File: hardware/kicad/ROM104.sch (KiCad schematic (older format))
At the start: 27 parts, among them J1 Screw_Terminal_01x12, J2 CAN, K1 DIPxx-1Cxx-51x, K2 DIPxx-1Cxx-51x, K3 DIPxx-1Cxx-51x, K4 DIPxx-1Cxx-51x, SW1 INSTANCE, SW2 BUS, U1 L293D, U2 MCP2551-I-P, U3 TMR-1211, U4 Teensy_3.2, U5 L293D

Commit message: Stuff
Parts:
- R12, R13, R14, R9: value 4K7 -> 470R
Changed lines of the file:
@@
 P 4400 800
 F 0 "R9" V 4450 1000 50  0000 R CNN
-F 1 "4K7" V 4400 800 39  0000 C CNN
+F 1 "470R" V 4400 800 39  0000 C CNN
 F 2 "Resistor_THT:R_Axial_DIN0204_L3.6mm_D1.6mm_P5.08mm_Horizontal" V 4330 800 50  0001 C CNN
 F 3 "~" H 4400 800 50  0001 C CNN
@@
 P 4400 1000
 F 0 "R12" V 4450 1250 50  0000 R CNN
-F 1 "4K7" V 4400 1000 39  0000 C CNN
+F 1 "470R" V 4400 1000 39  0000 C CNN
 F 2 "Resistor_THT:R_Axial_DIN0204_L3.6mm_D1.6mm_P5.08mm_Horizontal" V 4330 1000 50  0001 C CNN
 F 3 "~" H 4400 1000 50  0001 C CNN
@@
 P 4400 1200
 F 0 "R13" V 4450 1450 50  0000 R CNN
-F 1 "4K7" V 4400 1200 39  0000 C CNN
+F 1 "470R" V 4400 1200 39  0000 C CNN
 F 2 "Resistor_THT:R_Axial_DIN0204_L3.6mm_D1.6mm_P5.08mm_Horizontal" V 4330 1200 50  0001 C CNN
 F 3 "~" H 4400 1200 50  0001 C CNN
@@
 P 4400 1400
 F 0 "R14" V 4450 1650 50  0000 R CNN
-F 1 "4K7" V 4400 1400 39  0000 C CNN
+F 1 "470R" V 4400 1400 39  0000 C CNN
 F 2 "Resistor_THT:R_Axial_DIN0204_L3.6mm_D1.6mm_P5.08mm_Horizontal" V 4330 1400 50  0001 C CNN
 F 3 "~" H 4400 1400 50  0001 C CNN

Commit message: Tweaks
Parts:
- K1, K2, K3, K4: footprint Relay_THT:Relay_StandexMeder_DIP_LowProfile -> PDJR-connectors:PE014F05
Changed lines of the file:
@@
 F 0 "K2" H 1820 4354 50  0000 R CNN
 F 1 "DIPxx-1Cxx-51x" H 1820 4445 50  0000 R CNN
-F 2 "Relay_THT:Relay_StandexMeder_DIP_LowProfile" H 2700 4350 50  0001 L CNN
+F 2 "PDJR-connectors:PE014F05" H 2700 4350 50  0001 L CNN
 F 3 "https://standexelectronics.com/wp-content/uploads/datasheet_reed_relay_DIP.pdf" H 2250 4400 50  0001 C CNN
 	1    2250 4400
@@
 F 0 "K3" H 1820 5554 50  0000 R CNN
 F 1 "DIPxx-1Cxx-51x" H 1820 5645 50  0000 R CNN
-F 2 "Relay_THT:Relay_StandexMeder_DIP_LowProfile" H 2700 5550 50  0001 L CNN
+F 2 "PDJR-connectors:PE014F05" H 2700 5550 50  0001 L CNN
 F 3 "https://standexelectronics.com/wp-content/uploads/datasheet_reed_relay_DIP.pdf" H 2250 5600 50  0001 C CNN
 	1    2250 5600
@@
 F 0 "K1" H 1820 3354 50  0000 R CNN
 F 1 "DIPxx-1Cxx-51x" H 1820 3445 50  0000 R CNN
-F 2 "Relay_THT:Relay_StandexMeder_DIP_LowProfile" H 2700 3350 50  0001 L CNN
+F 2 "PDJR-connectors:PE014F05" H 2700 3350 50  0001 L CNN
 F 3 "https://standexelectronics.com/wp-content/uploads/datasheet_reed_relay_DIP.pdf" H 2250 3400 50  0001 C CNN
 	1    2250 3400
@@
 F 0 "K4" H 1820 6554 50  0000 R CNN
 F 1 "DIPxx-1Cxx-51x" H 1820 6645 50  0000 R CNN
-F 2 "Relay_THT:Relay_StandexMeder_DIP_LowProfile" H 2700 6550 50  0001 L CNN
+F 2 "PDJR-connectors:PE014F05" H 2700 6550 50  0001 L CNN
 F 3 "https://standexelectronics.com/wp-content/uploads/datasheet_reed_relay_DIP.pdf" H 2250 6600 50  0001 C CNN
 	1    2250 6600

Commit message: Switch PSU to 2W
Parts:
- removed U3: TMR-1211, PDJR-connectors:TMR-1-1211, symbol pdjr:TMR-1211
- added U3: TMR_2411, PDJR-connectors:TMR_2411, symbol pdjr:TMR_2411
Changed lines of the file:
@@
 	8350 5450 8350 5800
-$Comp
-L pdjr:TMR-1211 U3
-U 1 1 60ECA8BF
-P 8950 1050
-F 0 "U3" H 8950 1400 50  0000 C CNN
-F 1 "TMR-1211" H 8950 700 50  0000 C CNN
-F 2 "PDJR-connectors:TMR-1-1211" H 8950 700 50  0001 C CNN
-F 3 "" H 8950 550 50  0001 C CNN
-	1    8950 1050
-	-1   0    0    -1
-$EndComp
 $Comp
 L pdjr:Teensy_3.2 U4
@@
 Wire Wire Line
 	3650 5000 3650 7200
+$Comp
+L pdjr:TMR_2411 U3
+U 1 1 6327DB22
+P 8950 1050
+F 0 "U3" H 8950 1400 50  0000 C CNN
+F 1 "TMR_2411" H 8950 700 50  0000 C CNN
+F 2 "PDJR-connectors:TMR_2411" H 8950 700 50  0001 C CNN
+F 3 "" H 8950 550 50  0001 C CNN
+	1    8950 1050
+	-1   0    0    -1
+$EndComp
 $EndSCHEMATC

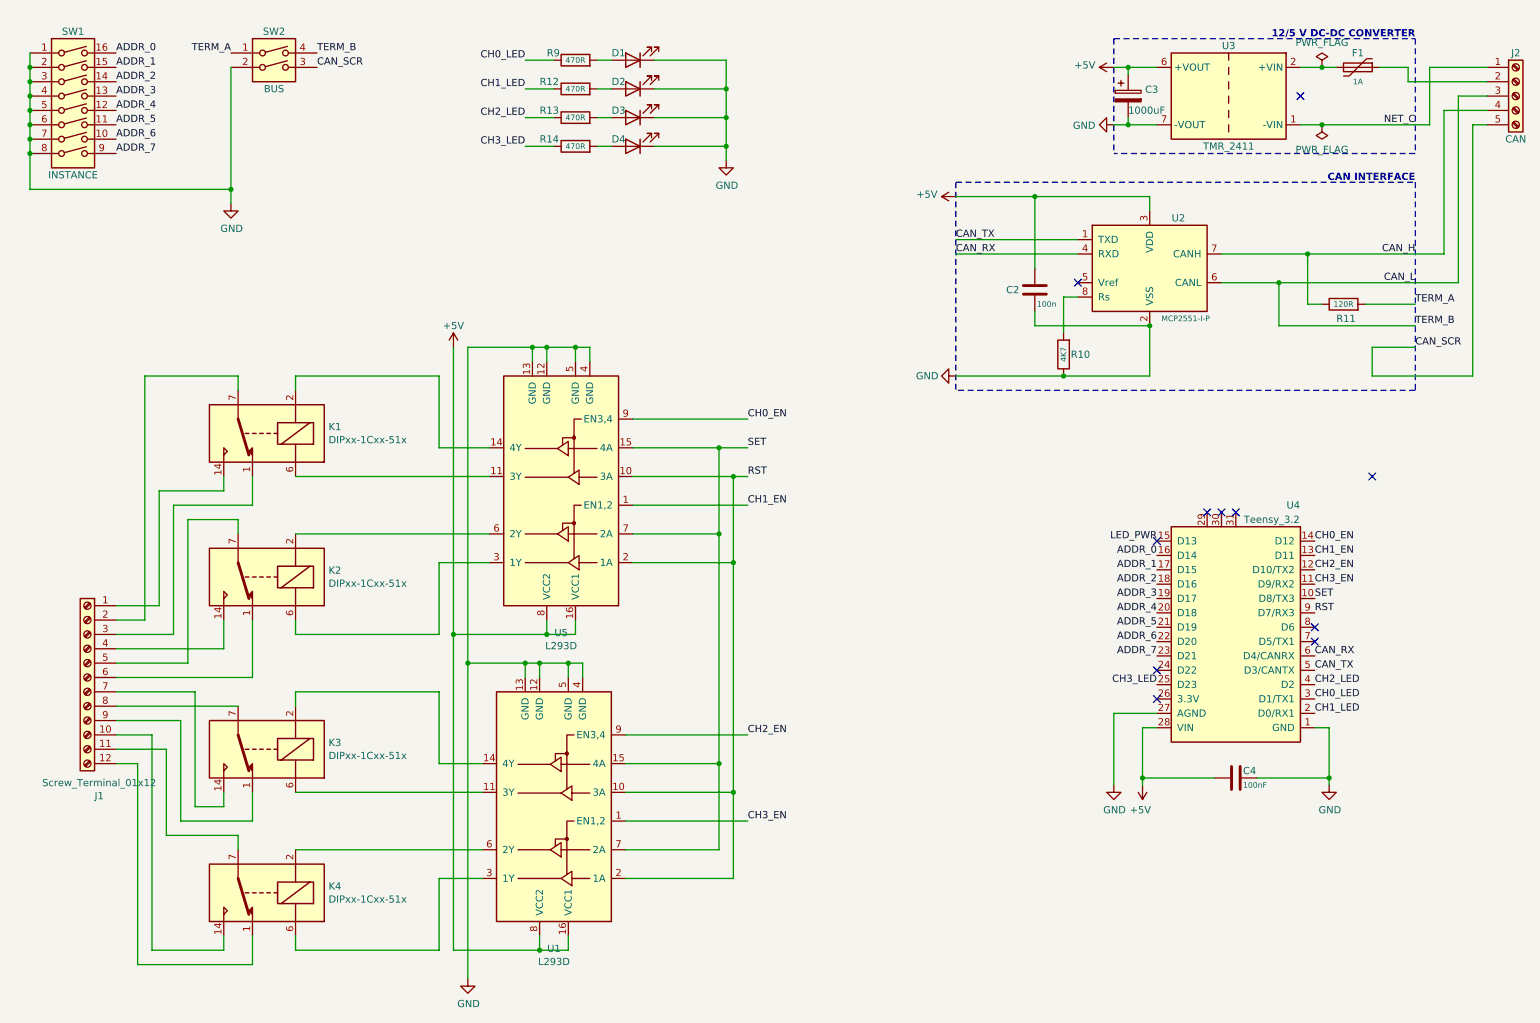
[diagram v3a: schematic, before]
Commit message: Change relay terminal
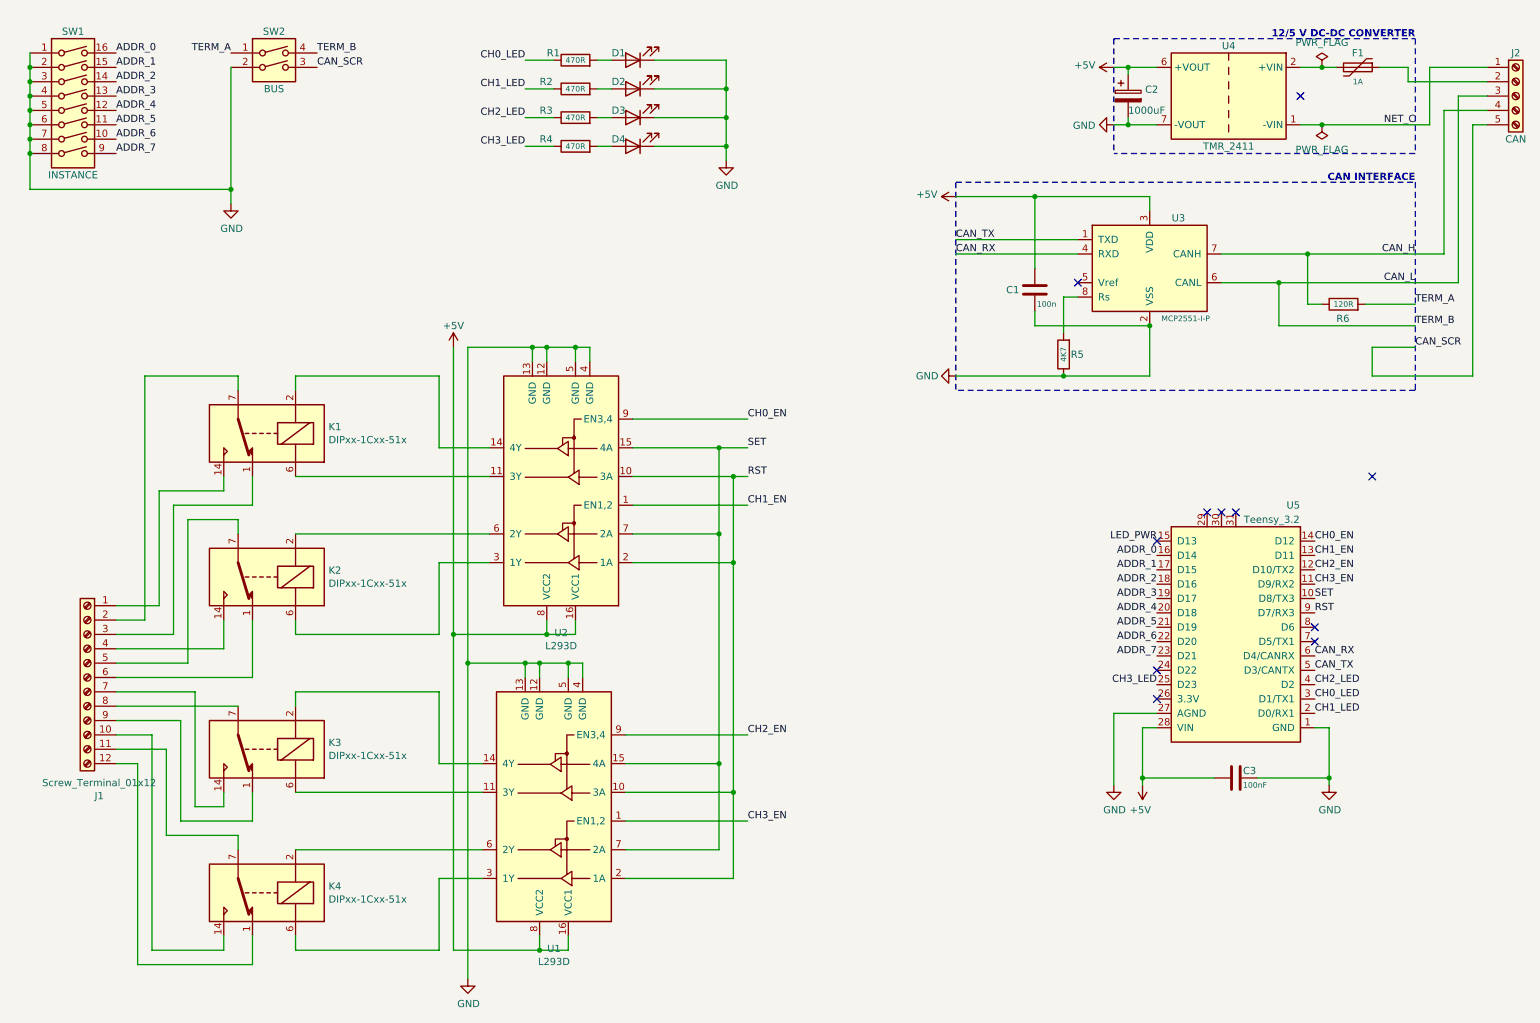
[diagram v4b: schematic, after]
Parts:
- J1: footprint TerminalBlock_WAGO:TerminalBlock_WAGO_236-112_1x12_P5.00mm_45Degree -> PDJR-connectors:WURTH-401B-12PIN
- renumbered C2 to C1, C3 to C2, C4 to C3, R9 to R1, R12 to R2, R13 to R3, R14 to R4, R10 to R5, R11 to R6, U5 to U2, U2 to U3, U3 to U4, U4 to U5
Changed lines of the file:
@@
 $EndDescr
 $Comp
-L Device:R R10
+L Device:R R5
 U 1 1 5F1E6C5E
 P 7800 2850
-F 0 "R10" H 7750 2850 50  0000 R CNN
+F 0 "R5" H 7750 2850 50  0000 R CNN
 F 1 "4K7" V 7800 2850 39  0000 C CNN
 F 2 "Resistor_THT:R_Axial_DIN0207_L6.3mm_D2.5mm_P7.62mm_Horizontal" V 7730 2850 50  0001 C CNN
@@
 $EndComp
 $Comp
-L Device:C C2
+L Device:C C1
 U 1 1 5F37E57C
 P 7600 2400
-F 0 "C2" H 7400 2400 50  0000 L CNN
+F 0 "C1" H 7400 2400 50  0000 L CNN
 F 1 "100n" H 7750 2300 39  0000 R CNN
 F 2 "Capacitor_THT:C_Rect_L4.6mm_W3.0mm_P2.50mm_MKS02_FKP02" H 7638 2250 50  0001 C CNN
@@
 $EndComp
 $Comp
-L Interface_CAN_LIN:MCP2551-I-P U2
+L Interface_CAN_LIN:MCP2551-I-P U3
 U 1 1 5F1D12F5
 P 8400 2250
-F 0 "U2" H 8600 2600 50  0000 C CNN
+F 0 "U3" H 8600 2600 50  0000 C CNN
 F 1 "MCP2551-I-P" H 8650 1900 39  0000 C CNN
 F 2 "Package_DIP:DIP-8_W7.62mm" H 8400 1750 50  0001 C CIN
@@
 $EndComp
 $Comp
-L Device:C C4
+L Device:C C3
 U 1 1 5F38A0E7
 P 9000 5800
-F 0 "C4" V 9050 5750 50  0000 R CNN
+F 0 "C3" V 9050 5750 50  0000 R CNN
 F 1 "100nF" V 8950 5750 39  0000 R CNN
 F 2 "Capacitor_THT:C_Rect_L4.6mm_W3.0mm_P2.50mm_MKS02_FKP02" H 9038 5650 50  0001 C CNN
@@
 CAN_SCR
 $Comp
-L power:+5V #PWR06
+L power:+5V #PWR07
 U 1 1 5FC3AC81
 P 8150 850
-F 0 "#PWR06" H 8150 700 50  0001 C CNN
+F 0 "#PWR07" H 8150 700 50  0001 C CNN
 F 1 "+5V" V 8165 978 50  0000 L CNN
 F 2 "" H 8150 850 50  0001 C CNN
@@
 $EndComp
 $Comp
-L power:GND #PWR07
+L power:GND #PWR08
 U 1 1 5FC3B74A
 P 8150 1250
-F 0 "#PWR07" H 8150 1000 50  0001 C CNN
+F 0 "#PWR08" H 8150 1000 50  0001 C CNN
 F 1 "GND" V 8155 1122 50  0000 R CNN
 F 2 "" H 8150 1250 50  0001 C CNN
@@
 $EndComp
 $Comp
-L power:+5V #PWR04
+L power:+5V #PWR05
 U 1 1 5FC442F6
 P 7050 1750
-F 0 "#PWR04" H 7050 1600 50  0001 C CNN
+F 0 "#PWR05" H 7050 1600 50  0001 C CNN
 F 1 "+5V" V 7065 1878 50  0000 L CNN
 F 2 "" H 7050 1750 50  0001 C CNN
@@
 $EndComp
 $Comp
-L power:GND #PWR05
+L power:GND #PWR06
 U 1 1 5FC44BAE
 P 7050 3000
-F 0 "#PWR05" H 7050 2750 50  0001 C CNN
+F 0 "#PWR06" H 7050 2750 50  0001 C CNN
 F 1 "GND" V 7050 2800 50  0000 C CNN
 F 2 "" H 7050 3000 50  0001 C CNN
@@
 	9950 3000 10650 3000
 $Comp
-L power:GND #PWR02
+L power:GND #PWR01
 U 1 1 6084E21C
 P 2000 1800
-F 0 "#PWR02" H 2000 1550 50  0001 C CNN
+F 0 "#PWR01" H 2000 1550 50  0001 C CNN
 F 1 "GND" H 2005 1627 50  0000 C CNN
 F 2 "" H 2000 1800 50  0001 C CNN
@@
 $EndComp
 $Comp
-L power:GND #PWR08
+L power:GND #PWR09
 U 1 1 6090D237
 P 8150 5850
-F 0 "#PWR08" H 8150 5600 50  0001 C CNN
+F 0 "#PWR09" H 8150 5600 50  0001 C CNN
 F 1 "GND" H 8155 5677 50  0000 C CNN
 F 2 "" H 8150 5850 50  0001 C CNN
@@
 $EndComp
 $Comp
-L power:+5V #PWR09
+L power:+5V #PWR010
 U 1 1 6090DC41
 P 8350 5850
-F 0 "#PWR09" H 8350 5700 50  0001 C CNN
+F 0 "#PWR010" H 8350 5700 50  0001 C CNN
 F 1 "+5V" H 8365 6023 50  0000 C CNN
 F 2 "" H 8350 5850 50  0001 C CNN
@@
 Connection ~ 8350 5800
 $Comp
-L power:GND #PWR010
+L power:GND #PWR011
 U 1 1 6096FBD9
 P 9650 5850
-F 0 "#PWR010" H 9650 5600 50  0001 C CNN
+F 0 "#PWR011" H 9650 5600 50  0001 C CNN
 F 1 "GND" H 9655 5677 50  0000 C CNN
 F 2 "" H 9650 5850 50  0001 C CNN
@@
 	8350 5450 8350 5800
 $Comp
-L pdjr:Teensy_3.2 U4
+L pdjr:Teensy_3.2 U5
 U 1 1 60F2AB82
 P 9550 5450
-F 0 "U4" H 9700 3900 50  0000 C CNN
+F 0 "U5" H 9700 3900 50  0000 C CNN
 F 1 "Teensy_3.2" H 9850 4000 50  0000 C CNN
 F 2 "Package_DIP:DIP-28_W15.24mm_LongPads" H 9550 5450 50  0001 C CNN
@@
 	9600 1250 10350 1250
 $Comp
-L Device:CP C3
+L Device:CP C2
 U 1 1 629FD333
 P 8250 1050
-F 0 "C3" H 8368 1096 50  0000 L CNN
+F 0 "C2" H 8368 1096 50  0000 L CNN
 F 1 "1000uF" H 8250 950 50  0000 L CNN
 F 2 "Capacitor_THT:CP_Radial_D8.0mm_P5.00mm" H 8288 900 50  0001 C CNN
@@
 NoConn ~ 8800 3950
 $Comp
-L Device:R R11
+L Device:R R6
 U 1 1 62A3BFE8
 P 9750 2500
-F 0 "R11" V 9650 2550 50  0000 R CNN
+F 0 "R6" V 9650 2550 50  0000 R CNN
 F 1 "120R" V 9750 2500 39  0000 C CNN
 F 2 "Resistor_THT:R_Axial_DIN0207_L6.3mm_D2.5mm_P7.62mm_Horizontal" V 9680 2500 50  0001 C CNN
@@
 F 0 "J1" H 918 4275 50  0000 C CNN
 F 1 "Screw_Terminal_01x12" H 918 4366 50  0000 C CNN
-F 2 "TerminalBlock_WAGO:TerminalBlock_WAGO_236-112_1x12_P5.00mm_45Degree" H 1000 5100 50  0001 C CNN
+F 2 "PDJR-connectors:WURTH-401B-12PIN" H 1000 5100 50  0001 C CNN
 F 3 "~" H 1000 5100 50  0001 C CNN
 	1    1000 5100
@@
 CH3_LED
 $Comp
-L Device:R R9
+L Device:R R1
 U 1 1 631C1A0C
 P 4400 800
-F 0 "R9" V 4450 1000 50  0000 R CNN
+F 0 "R1" V 4450 1000 50  0000 R CNN
 F 1 "470R" V 4400 800 39  0000 C CNN
 F 2 "Resistor_THT:R_Axial_DIN0204_L3.6mm_D1.6mm_P5.08mm_Horizontal" V 4330 800 50  0001 C CNN
@@
 	5450 800  5450 1000
 $Comp
-L Device:R R12
+L Device:R R2
 U 1 1 631D6F98
 P 4400 1000
-F 0 "R12" V 4450 1250 50  0000 R CNN
+F 0 "R2" V 4450 1250 50  0000 R CNN
 F 1 "470R" V 4400 1000 39  0000 C CNN
 F 2 "Resistor_THT:R_Axial_DIN0204_L3.6mm_D1.6mm_P5.08mm_Horizontal" V 4330 1000 50  0001 C CNN
@@
 $EndComp
 $Comp
-L Device:R R13
+L Device:R R3
 U 1 1 631D739B
 P 4400 1200
-F 0 "R13" V 4450 1450 50  0000 R CNN
+F 0 "R3" V 4450 1450 50  0000 R CNN
 F 1 "470R" V 4400 1200 39  0000 C CNN
 F 2 "Resistor_THT:R_Axial_DIN0204_L3.6mm_D1.6mm_P5.08mm_Horizontal" V 4330 1200 50  0001 C CNN
@@
 $EndComp
 $Comp
-L Device:R R14
+L Device:R R4
 U 1 1 631D7696
 P 4400 1400
-F 0 "R14" V 4450 1650 50  0000 R CNN
+F 0 "R4" V 4450 1650 50  0000 R CNN
 F 1 "470R" V 4400 1400 39  0000 C CNN
 F 2 "Resistor_THT:R_Axial_DIN0204_L3.6mm_D1.6mm_P5.08mm_Horizontal" V 4330 1400 50  0001 C CNN
@@
 	5450 1400 5450 1500
 $Comp
-L power:GND #PWR01
+L power:GND #PWR04
 U 1 1 632040BF
 P 5450 1500
-F 0 "#PWR01" H 5450 1250 50  0001 C CNN
+F 0 "#PWR04" H 5450 1250 50  0001 C CNN
 F 1 "GND" H 5455 1327 50  0000 C CNN
 F 2 "" H 5450 1500 50  0001 C CNN
@@
 CH3_LED
 $Comp
-L Driver_Motor:L293D U5
+L Driver_Motor:L293D U2
 U 1 1 631FC180
 P 4300 3700
-F 0 "U5" H 4300 4789 50  0000 C CNN
+F 0 "U2" H 4300 4789 50  0000 C CNN
 F 1 "L293D" H 4300 4880 50  0000 C CNN
 F 2 "Package_DIP:DIP-16_W7.62mm" H 4550 2950 50  0001 L CNN
@@
 	3550 2800 3550 4800
 $Comp
-L power:+5V #PWR03
+L power:+5V #PWR02
 U 1 1 634BDEB3
 P 3550 2800
-F 0 "#PWR03" H 3550 2650 50  0001 C CNN
+F 0 "#PWR02" H 3550 2650 50  0001 C CNN
 F 1 "+5V" H 3550 2950 50  0000 C CNN
 F 2 "" H 3550 2800 50  0001 C CNN
@@
 Connection ~ 4100 2800
 $Comp
-L power:GND #PWR011
+L power:GND #PWR03
 U 1 1 6365743E
 P 3650 7200
-F 0 "#PWR011" H 3650 6950 50  0001 C CNN
+F 0 "#PWR03" H 3650 6950 50  0001 C CNN
 F 1 "GND" H 3655 7027 50  0000 C CNN
 F 2 "" H 3650 7200 50  0001 C CNN
@@
 	3650 5000 3650 7200
 $Comp
-L pdjr:TMR_2411 U3
+L pdjr:TMR_2411 U4
 U 1 1 6327DB22
 P 8950 1050
-F 0 "U3" H 8950 1400 50  0000 C CNN
+F 0 "U4" H 8950 1400 50  0000 C CNN
 F 1 "TMR_2411" H 8950 700 50  0000 C CNN
 F 2 "PDJR-connectors:TMR_2411" H 8950 700 50  0001 C CNN

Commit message: Change resistor footprints
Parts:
- R5: footprint Resistor_THT:R_Axial_DIN0207_L6.3mm_D2.5mm_P7.62mm_Horizontal -> Resistor_THT:R_Axial_DIN0204_L3.6mm_D1.6mm_P5.08mm_Horizontal
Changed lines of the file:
@@
 F 0 "R5" H 7750 2850 50  0000 R CNN
 F 1 "4K7" V 7800 2850 39  0000 C CNN
-F 2 "Resistor_THT:R_Axial_DIN0207_L6.3mm_D2.5mm_P7.62mm_Horizontal" V 7730 2850 50  0001 C CNN
+F 2 "Resistor_THT:R_Axial_DIN0204_L3.6mm_D1.6mm_P5.08mm_Horizontal" V 7730 2850 50  0001 C CNN
 F 3 "~" H 7800 2850 50  0001 C CNN
 	1    7800 2850

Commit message: Restore 1/4W resistor footprints
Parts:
- R1, R2, R3, R4, R5: footprint Resistor_THT:R_Axial_DIN0204_L3.6mm_D1.6mm_P5.08mm_Horizontal -> Resistor_THT:R_Axial_DIN0207_L6.3mm_D2.5mm_P7.62mm_Horizontal
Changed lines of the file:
@@
 F 0 "R5" H 7750 2850 50  0000 R CNN
 F 1 "4K7" V 7800 2850 39  0000 C CNN
-F 2 "Resistor_THT:R_Axial_DIN0204_L3.6mm_D1.6mm_P5.08mm_Horizontal" V 7730 2850 50  0001 C CNN
+F 2 "Resistor_THT:R_Axial_DIN0207_L6.3mm_D2.5mm_P7.62mm_Horizontal" V 7730 2850 50  0001 C CNN
 F 3 "~" H 7800 2850 50  0001 C CNN
 	1    7800 2850
@@
 F 0 "R1" V 4450 1000 50  0000 R CNN
 F 1 "470R" V 4400 800 39  0000 C CNN
-F 2 "Resistor_THT:R_Axial_DIN0204_L3.6mm_D1.6mm_P5.08mm_Horizontal" V 4330 800 50  0001 C CNN
+F 2 "Resistor_THT:R_Axial_DIN0207_L6.3mm_D2.5mm_P7.62mm_Horizontal" V 4330 800 50  0001 C CNN
 F 3 "~" H 4400 800 50  0001 C CNN
 	1    4400 800
@@
 F 0 "R2" V 4450 1250 50  0000 R CNN
 F 1 "470R" V 4400 1000 39  0000 C CNN
-F 2 "Resistor_THT:R_Axial_DIN0204_L3.6mm_D1.6mm_P5.08mm_Horizontal" V 4330 1000 50  0001 C CNN
+F 2 "Resistor_THT:R_Axial_DIN0207_L6.3mm_D2.5mm_P7.62mm_Horizontal" V 4330 1000 50  0001 C CNN
 F 3 "~" H 4400 1000 50  0001 C CNN
 	1    4400 1000
@@
 F 0 "R3" V 4450 1450 50  0000 R CNN
 F 1 "470R" V 4400 1200 39  0000 C CNN
-F 2 "Resistor_THT:R_Axial_DIN0204_L3.6mm_D1.6mm_P5.08mm_Horizontal" V 4330 1200 50  0001 C CNN
+F 2 "Resistor_THT:R_Axial_DIN0207_L6.3mm_D2.5mm_P7.62mm_Horizontal" V 4330 1200 50  0001 C CNN
 F 3 "~" H 4400 1200 50  0001 C CNN
 	1    4400 1200
@@
 F 0 "R4" V 4450 1650 50  0000 R CNN
 F 1 "470R" V 4400 1400 39  0000 C CNN
-F 2 "Resistor_THT:R_Axial_DIN0204_L3.6mm_D1.6mm_P5.08mm_Horizontal" V 4330 1400 50  0001 C CNN
+F 2 "Resistor_THT:R_Axial_DIN0207_L6.3mm_D2.5mm_P7.62mm_Horizontal" V 4330 1400 50  0001 C CNN
 F 3 "~" H 4400 1400 50  0001 C CNN
 	1    4400 1400
